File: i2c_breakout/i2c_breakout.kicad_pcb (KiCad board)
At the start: 2 copper layers, 45.2 x 10 mm, 8 parts, among them J1 Conn_01x02_Male, J2 Conn_01x04_Male, J3 Conn_01x04_Male, J4 Conn_01x04_Male, J5 Conn_01x04_Male, J6 Conn_01x04_Male, J7 5V, J8 GND

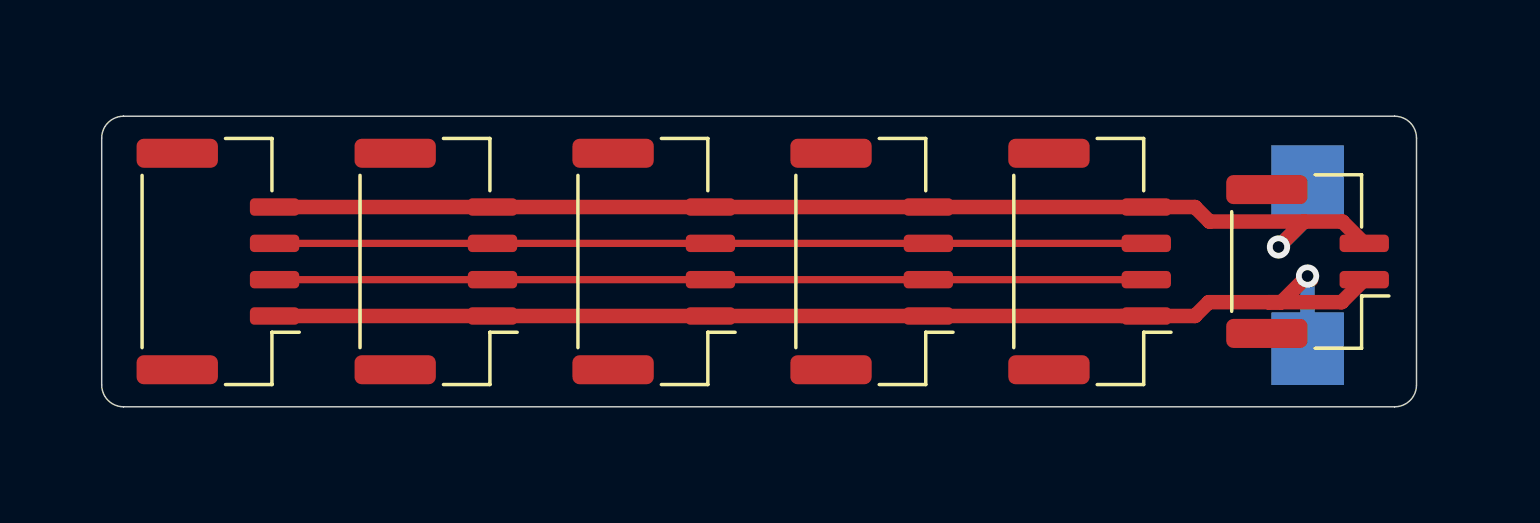
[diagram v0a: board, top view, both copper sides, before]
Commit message: Added a ground plane where it was forgotten
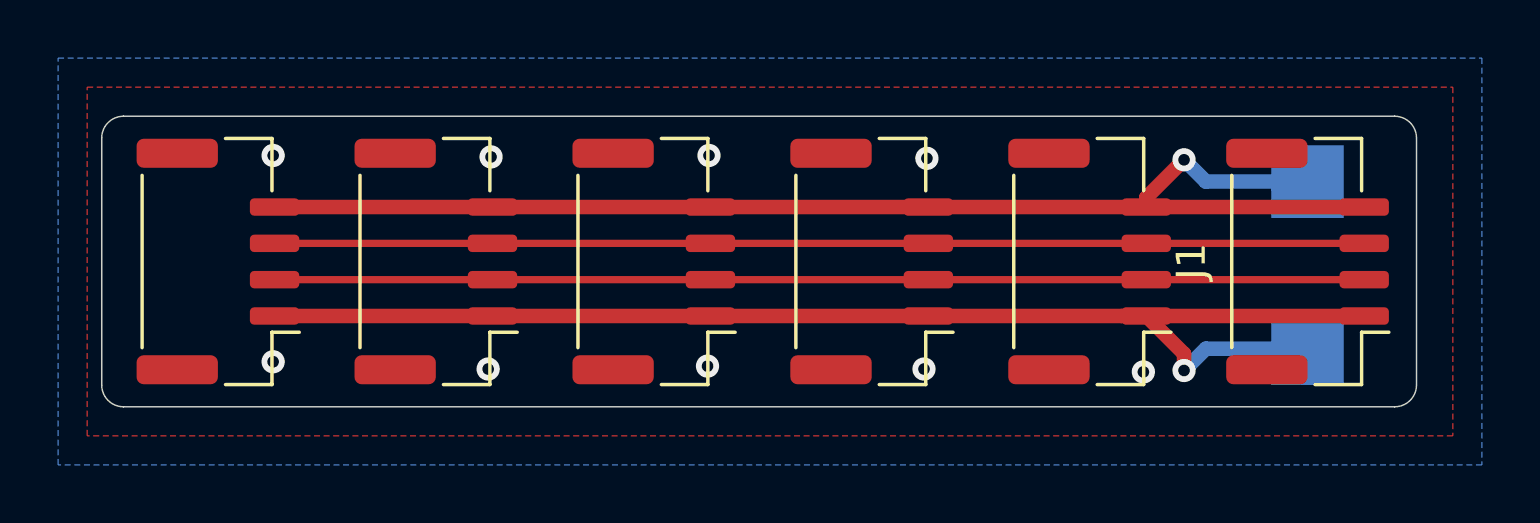
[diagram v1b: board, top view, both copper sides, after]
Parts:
- J1: value Conn_01x02_Male -> Conn_01x04_Male; footprint Connector_JST:JST_GH_BM02B-GHS-TBT_1x02-1MP_P1.25mm_Vertical -> Connector_JST:JST_GH_BM04B-GHS-TBT_1x04-1MP_P1.25mm_Vertical
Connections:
- J1 pad 2: Earth -> Net-(J1-Pad2)
- J2 pad 2: Net-(J2-Pad2) -> Net-(J1-Pad2)
- J2 pad 3: Net-(J2-Pad3) -> Net-(J1-Pad3)
- J3 pad 2: Net-(J2-Pad2) -> Net-(J1-Pad2)
- J3 pad 3: Net-(J2-Pad3) -> Net-(J1-Pad3)
- J4 pad 2: Net-(J2-Pad2) -> Net-(J1-Pad2)
- J4 pad 3: Net-(J2-Pad3) -> Net-(J1-Pad3)
- J5 pad 2: Net-(J2-Pad2) -> Net-(J1-Pad2)
- J5 pad 3: Net-(J2-Pad3) -> Net-(J1-Pad3)
- J6 pad 2: Net-(J2-Pad2) -> Net-(J1-Pad2)
- J6 pad 3: Net-(J2-Pad3) -> Net-(J1-Pad3)
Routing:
- net Net-(J1-Pad3): track 0.00 -> 37.5 mm
- net Net-(J1-Pad2): track 0.00 -> 37.5 mm
- net Net-(J2-Pad3): track 30.0 -> 0.00 mm
- net Net-(J2-Pad2): track 30.0 -> 0.00 mm
- net Earth: track 43.3 -> 45.6 mm, vias 1 -> 10
- net +5V: track 42.4 -> 44.5 mm
- added copper zone on B.Cu, net Earth
- added copper zone on F.Cu, net Earth
